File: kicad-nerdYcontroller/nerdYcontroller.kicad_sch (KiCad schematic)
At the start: 1 part, among them U101 RP2040

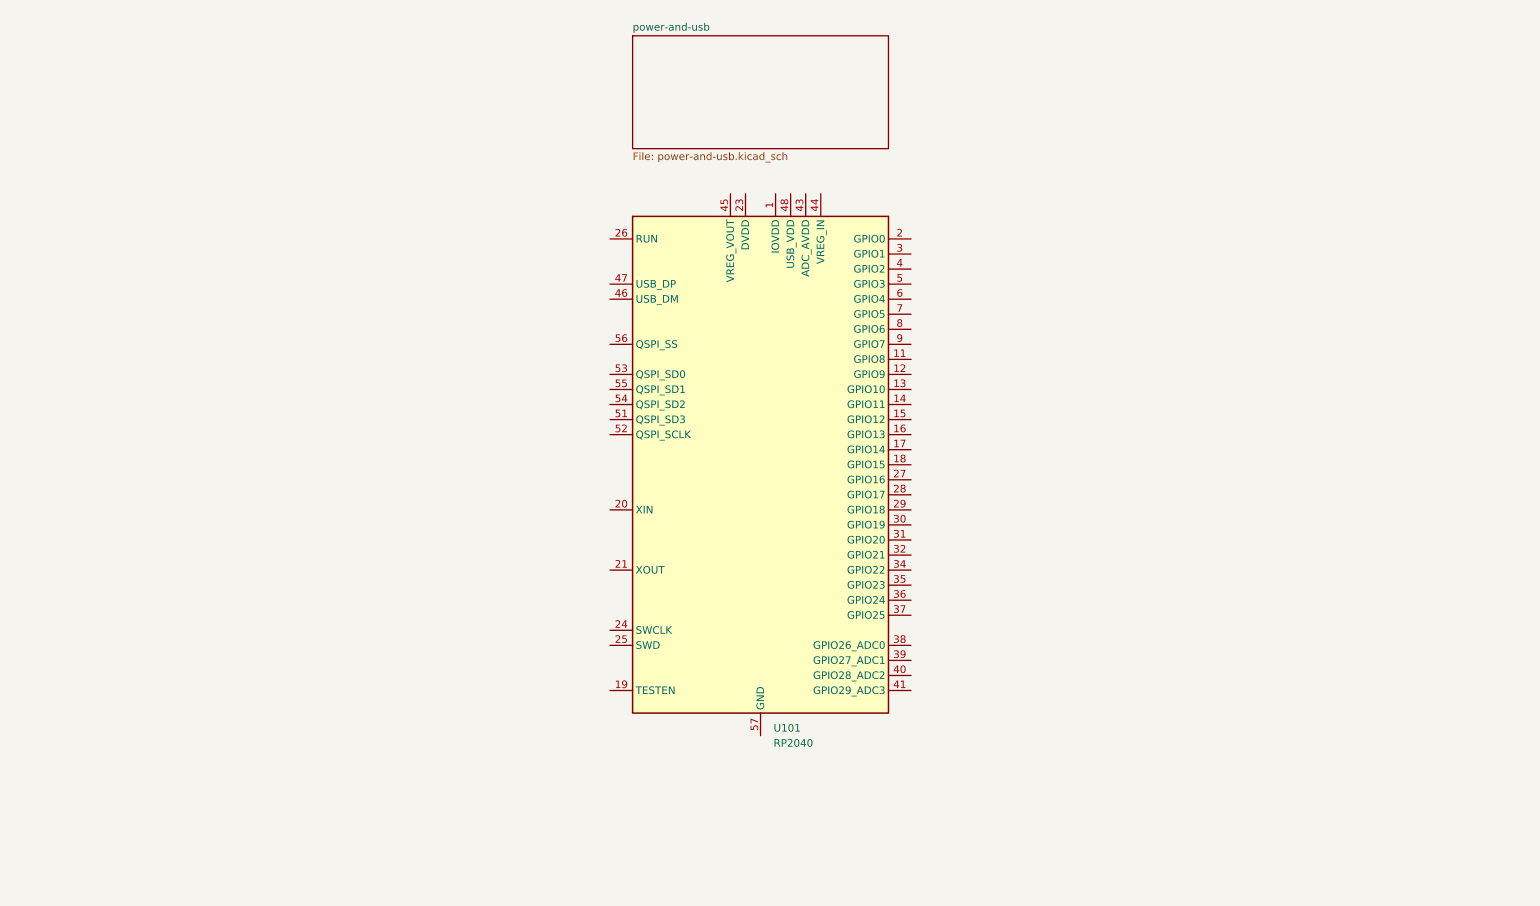
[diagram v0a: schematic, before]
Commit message: Adding kicad-nerdYController
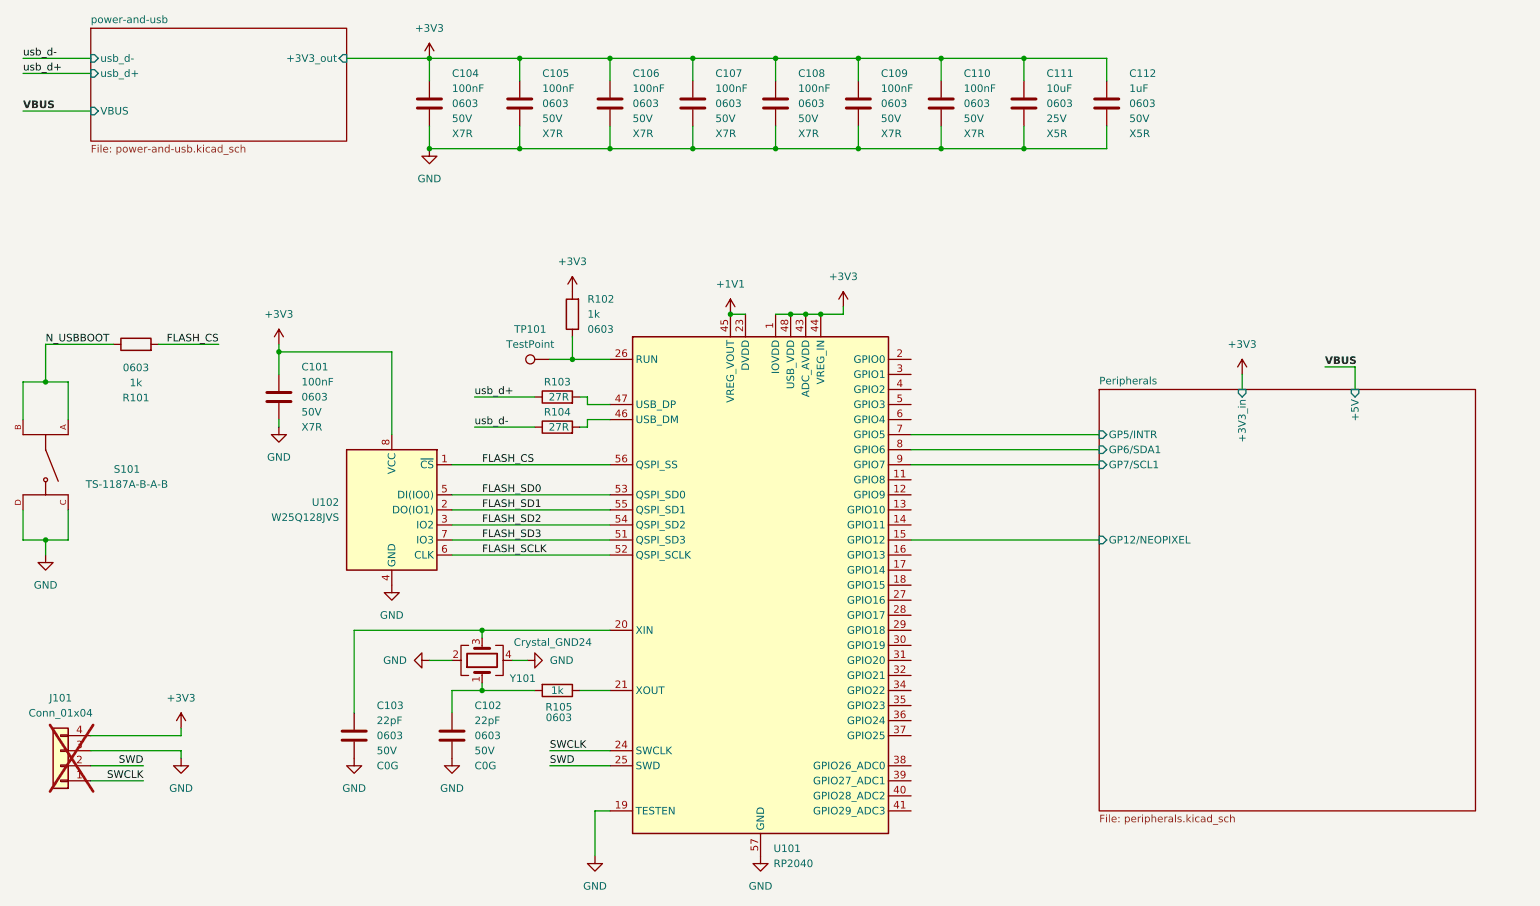
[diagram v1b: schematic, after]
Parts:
- added C101, C104, C105, C106, C107, C108, C109, C110: 100nF, Capacitor_SMD:C_0603_1608Metric, symbol kidslab:C-100nF-0603-50V
- added C102, C103: 22pF, Capacitor_SMD:C_0603_1608Metric, symbol kidslab:C-22pF-0603-50V
- added C111: 10uF, Capacitor_SMD:C_0603_1608Metric, symbol kidslab:C-10uF-0603-25V
- added C112: 1uF, Capacitor_SMD:C_0603_1608Metric, symbol kidslab:C-1uF-0603-25V_1
- added J101: Conn_01x04, symbol Connector_Generic:Conn_01x04
- added R101, R102, R105: 1k, Resistor_SMD:R_0603_1608Metric, symbol kidslab:R-1k-0603
- added R103, R104: 27R, Resistor_SMD:R_0603_1608Metric, symbol kidslab:R-27R-0603
- added S101: TS-1187A-B-A-B, kidslab:SW_TS-1187A-B-A-B, symbol kidslab:TS-1187A-B-A-B
- added TP101: TestPoint, TestPoint:TestPoint_Pad_D1.5mm, symbol Connector:TestPoint
- added U102: W25Q128JVS, Package_SO:SOIC-8_5.23x5.23mm_P1.27mm, symbol kidslab:W25Q128JVS
- added Y101: Crystal_GND24, Crystal:Crystal_SMD_3225-4Pin_3.2x2.5mm, symbol kidslab:X322512MSB4SI
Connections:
- net +3V3: now reaches U101.1 (IOVDD), U101.10 (IOVDD), U101.22 (IOVDD), U101.33 (IOVDD), U101.42 (IOVDD), U101.49 (IOVDD)
- net +3V3: now also U101.43 (ADC_AVDD), U101.44 (VREG_IN), U101.48 (USB_VDD), C101.1, C104.1, C105.1, C106.1, C107.1, C108.1, C109.1, C110.1, C111.1, C112.1, J101.4 (Pin_4), R102.2, U102.8 (VCC)
- net Peripherals/GP12/NEOPIXEL: now reaches U101.15 (GPIO12)
- net GND: now reaches U101.19 (TESTEN)
- net GND: now also U101.57 (GND), C101.2, C102.2, C103.2, C104.2, C105.2, C106.2, C107.2, C108.2, C109.2, C110.2, C111.2, C112.2, J101.3 (Pin_3), S101.C, S101.D, U102.4 (GND), Y101.2, Y101.4
- net at U101.20 (XIN): now also C103.1, Y101.3
- net at U101.21 (XOUT): now also R105.1
- net +1V1: now reaches U101.23 (DVDD), U101.50 (DVDD)
- net +1V1: now also U101.45 (VREG_VOUT)
- net SWCLK: now reaches U101.24 (SWCLK)
- net SWCLK: now also J101.1 (Pin_1)
- net SWD: now reaches U101.25 (SWD)
- net SWD: now also J101.2 (Pin_2)
- net at U101.26 (RUN): now also R102.1, TP101.1
- net at U101.46 (USB_DM): now also R104.2
- net at U101.47 (USB_DP): now also R103.2
- net FLASH_SD3: now reaches U101.51 (QSPI_SD3)
- net FLASH_SD3: now also U102.7 (IO3)
- net FLASH_SCLK: now reaches U101.52 (QSPI_SCLK)
- net FLASH_SCLK: now also U102.6 (CLK)
- net FLASH_SD0: now reaches U101.53 (QSPI_SD0)
- net FLASH_SD0: now also U102.5 (DI(IO0))
- net FLASH_SD2: now reaches U101.54 (QSPI_SD2)
- net FLASH_SD2: now also U102.3 (IO2)
- net FLASH_SD1: now reaches U101.55 (QSPI_SD1)
- net FLASH_SD1: now also U102.2 (DO(IO1))
- net FLASH_CS: now reaches U101.56 (QSPI_SS)
- net FLASH_CS: now also R101.2, U102.1 (~{CS})
- net Peripherals/GP5/INTR: now reaches U101.7 (GPIO5)
- net Peripherals/GP6/SDA1: now reaches U101.8 (GPIO6)
- net Peripherals/GP7/SCL1: now reaches U101.9 (GPIO7)
- new net: C102.1, R105.2, Y101.1
- new net N_USBBOOT: R101.1, S101.A, S101.B
- new net usb_d+: R103.1
- new net usb_d-: R104.1
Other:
- added sheet Peripherals (peripherals.kicad_sch)
- sheet power-and-usb ports: added +3V3_out, VBUS, usb_d+, usb_d-; removed none
- moved on the sheet: U101

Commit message: Adding KiCad files for first controller production.
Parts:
- removed C104, C105, C106, C107, C108, C109, C110: 100nF, Capacitor_SMD:C_0603_1608Metric, symbol kidslab:C-100nF-0603-50V
- removed J101: Conn_01x04, symbol Connector_Generic:Conn_01x04
- removed TP101: TestPoint, TestPoint:TestPoint_Pad_D1.5mm, symbol Connector:TestPoint
- added C104, C105, C106, C107, C108, C109, C110: 100nF, Capacitor_SMD:C_0402_1005Metric, symbol kidslab:C-100nF-0402-25V
- added C113, C114: 100nF, Capacitor_SMD:C_0603_1608Metric, symbol kidslab:C-100nF-0603-50V
- added C115: 1uF, Capacitor_SMD:C_0603_1608Metric, symbol kidslab:C-1uF-0603-25V_1
- U102: footprint Package_SO:SOIC-8_5.23x5.23mm_P1.27mm -> kidslab:SOIC-8_5.23x5.23mm_P1.27mm
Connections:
- net +1V1: now also C113.1, C114.1, C115.1
- net +3V3: now also C104.2, C105.2, C106.2, C107.2, C108.2, C109.2, C110.2
- net GND: now also C104.1, C105.1, C106.1, C107.1, C108.1, C109.1, C110.1, C113.2, C114.2, C115.2
- net d+: now reaches R103.2, U101.47 (USB_DP)
- net Peripherals/GP8/Grove_D1: now reaches U101.11 (GPIO8)
- net Peripherals/GP9/Grove_D0: now reaches U101.12 (GPIO9)
- net Peripherals/GP10/SERVO_0: now reaches U101.13 (GPIO10)
- net Peripherals/GP11/SERVO_1: now reaches U101.14 (GPIO11)
- net Peripherals/GP13/INTR: now reaches U101.16 (GPIO13)
- net Peripherals/GP14/ArrowLeft: now reaches U101.17 (GPIO14)
- net Peripherals/GP15/ArrowUp: now reaches U101.18 (GPIO15)
- net Peripherals/GP0: now reaches U101.2 (GPIO0)
- net Peripherals/GP16/ArrowRight: now reaches U101.27 (GPIO16)
- net Peripherals/GP17/ArrowDown: now reaches U101.28 (GPIO17)
- net Peripherals/GP18: now reaches U101.29 (GPIO18)
- net Peripherals/GP1: now reaches U101.3 (GPIO1)
- net Peripherals/GP19: now reaches U101.30 (GPIO19)
- net Peripherals/GP20/Buzzer: now reaches U101.31 (GPIO20)
- net Peripherals/GP21: now reaches U101.32 (GPIO21)
- net Peripherals/GP22: now reaches U101.34 (GPIO22)
- net Peripherals/GP23: now reaches U101.35 (GPIO23)
- net Peripherals/GP24: now reaches U101.36 (GPIO24)
- net Peripherals/GP25/LED: now reaches U101.37 (GPIO25)
- net Peripherals/GP26: now reaches U101.38 (GPIO26_ADC0)
- net Peripherals/GP27: now reaches U101.39 (GPIO27_ADC1)
- net Peripherals/GP2: now reaches U101.4 (GPIO2)
- net Peripherals/GP28: now reaches U101.40 (GPIO28_ADC2)
- net Peripherals/GP29/MIC_OUT: now reaches U101.41 (GPIO29_ADC3)
- net d-: now reaches R104.2, U101.46 (USB_DM)
- net Peripherals/GP3: now reaches U101.5 (GPIO3)
- net Peripherals/GP4/SERVO_2: now reaches U101.6 (GPIO4)
- net Peripherals/GP5/INTR renamed Peripherals/GP5/SERVO_3
- net Peripherals/GP6/SDA1 renamed Peripherals/GP6/IMU_SDA
- net Peripherals/GP7/SCL1 renamed Peripherals/GP7/IMU_SCL
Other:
- sheet Peripherals ports: added GP0, GP1, GP10/SERVO_0, GP11/SERVO_1, GP13/INTR, GP14/ArrowLeft, GP15/ArrowUp, GP16/ArrowRight, GP17/ArrowDown, GP18, GP19, GP2, GP20/Buzzer, GP21, GP22, GP23, GP24, GP25/LED, GP26, GP27, GP28, GP29/MIC_OUT, GP3, GP4/SERVO_2, GP5/SERVO_3, GP6/IMU_SDA, GP7/IMU_SCL, GP8/Grove_D1, GP9/Grove_D0, SWCLK, SWD, VBUS; removed +5V, GP5/INTR, GP6/SDA1, GP7/SCL1
- moved on the sheet: R103, R104
